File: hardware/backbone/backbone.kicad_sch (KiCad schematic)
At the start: 68 parts, among them J1 M20-7810645R, J140 M20-7810645R, J2 FROM_PREVIOUS, J3 M20-7810645R, J4 SM04B-SRSS-TB(LF)(SN), J5 FH12-24S-0.5SH(55), J9 TO NEXT, Q2 AO3401A, U1 ESP32-S3-WROOM-1_1U_FlexyPin_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, U10 ME6211C15M5G-N, U11 SN74LVC1G125DBVR, U2 SN65HVD230DR, U3 HC-TYPE-C-16P-01A, U4 AP2112K-3.3TRG1, U5 AP2112K-3.3TRG1, U8 G3VM-61VY3, U9 ME6211C28M5G-N

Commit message: Use power symbols and generic FPC expansion names
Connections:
- net CAM_1V5 renamed +1V5
- net CAM_2V8 renamed +2V8
- net CAM_PWDN renamed FPC_PULLDOWN
- net CAM_RESET_N renamed FPC_PULLUP
- net CAM_XCLK renamed FPC_CLK
- net CAM_XCLK_DRV renamed FPC_CLK_DRV
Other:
- note added: "+1V5"
- note added: "+2V8"
- note added: "AUXILIARY 1.5 V REGULATOR"
- note added: "AUXILIARY 2.8 V REGULATOR"
- note added: "BUFFERED CLOCK - 3.3 V TO 2.8 V"
- note added: "Buffer GPIO15; place R30 close to U11 output."
- note added: "C79/C80: +2V8 decoupling. C81: +1V5 decoupling."
- note added: "CLK_OUT"
- note added: "Check peripheral pinout, voltages and flex orientation."
- note added: "EXPANSION - 24-PIN FPC"
- note added: "FPC BIAS RESISTORS"
- note added: "FPC shares I2C on GPIO4/5; pull-ups to 3.3 V."
- note added: "FPC signals, fixed bias pins and voltage limits: see project documentation."
- note added: "FPC_PULLDOWN: 10k to GND"
- note added: "FPC_PULLUP: 10k to +2V8"
- note added: "Fixed auxiliary rails: 2.8 V / 1.5 V. Check peripheral voltage requirements."
- note added: "Fixed pull-up / pull-down; no MCU control assigned."
- note added: "GPIO1"
- note added: "GPIO17"
- note added: "GPIO18"
- note added: "GPIO2"
- note added: "GPIO21"
- note added: "GPIO38"
- note added: "GPIO39"
- note added: "GPIO40"
- note added: "GPIO41"
- note added: "GPIO42"
- note added: "GPIO6"
- note added: "PULLDOWN"
- note added: "PULLUP"
- note removed: "AVDD 2.8V"
- note removed: "Buffer XCLK; place R30 close to U11 output."
- note removed: "C79: AVDD; C80: DOVDD; C81: DVDD."
- note removed: "CAMERA 1.5 V REGULATOR"
- note removed: "CAMERA 2.8 V REGULATOR"
- note removed: "CAMERA CLOCK - 3.3 V TO 2.8 V"
- note removed: "CAMERA CONTROL DEFAULTS"
- note removed: "CAMERA DVP - 24-PIN FPC"
- note removed: "Camera SCCB shares GPIO4/5 directly; pull-ups to 3.3 V."
- note removed: "D0 / Y2"
- note removed: "D1 / Y3"
- note removed: "D2 / Y4"
- note removed: "D3 / Y5"
- note removed: "D4 / Y6"
- note removed: "D5 / Y7"
- note removed: "D6 / Y8"
- note removed: "D7 / Y9"
- note removed: "DOVDD 2.8V"
- note removed: "DVDD 1.5V"
- note removed: "ESP32-S3-EYE pinout. Verify the actual flex orientation."
- note removed: "Fixed camera rails: 2.8 V / 1.5 V. Qualify each camera module before use."
- note removed: "GPIO assignments and electrical limits: hardware/backbone/CAMERA-V3.md"
- note removed: "HREF"
- note removed: "No MCU GPIO assigned to RESET or PWDN."
- note removed: "PCLK"
- note removed: "PWDN"
- note removed: "PWDN: low = active"
- note removed: "RESET_N"
- note removed: "RESET_N: high = run"
- note removed: "VSYNC"
- note removed: "XCLK"

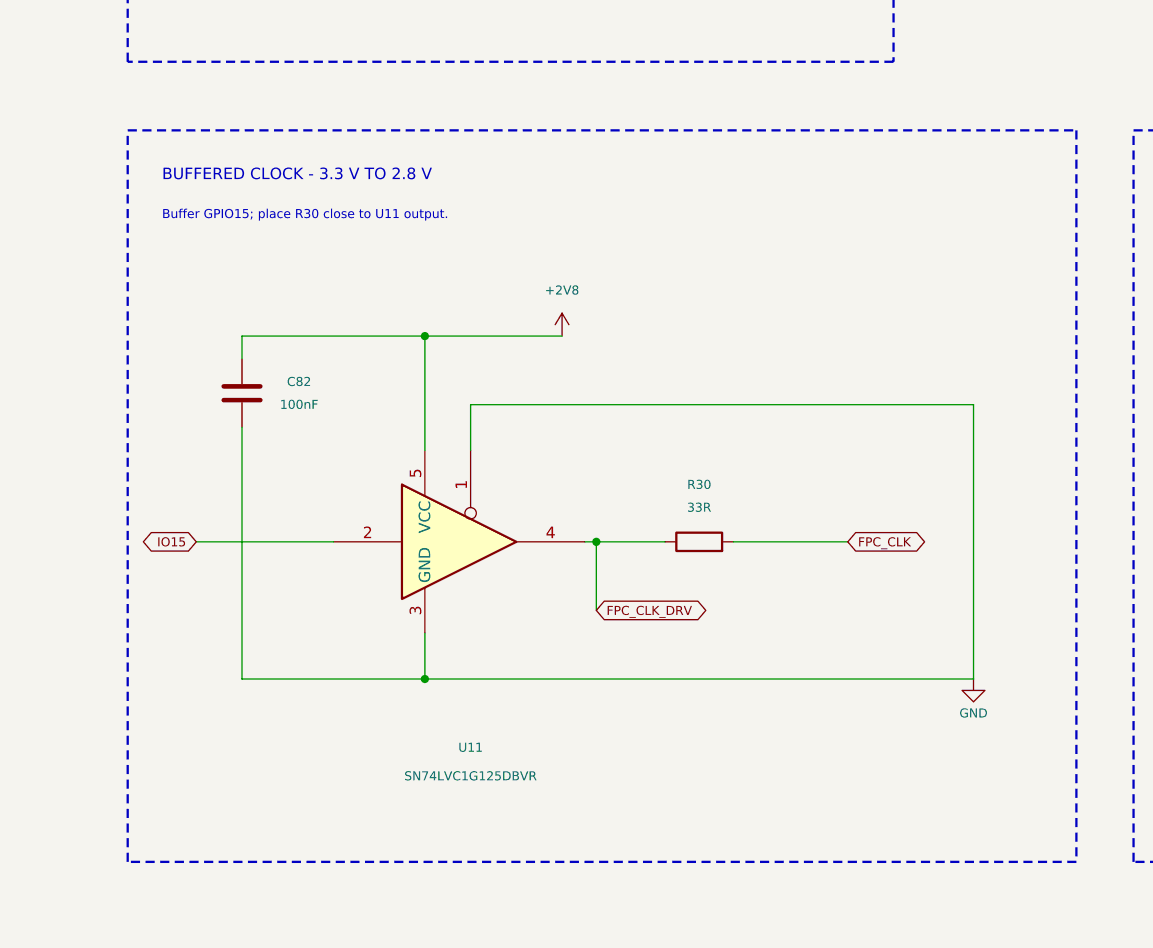
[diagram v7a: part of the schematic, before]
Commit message: Match Espressif camera clock path without added buffer
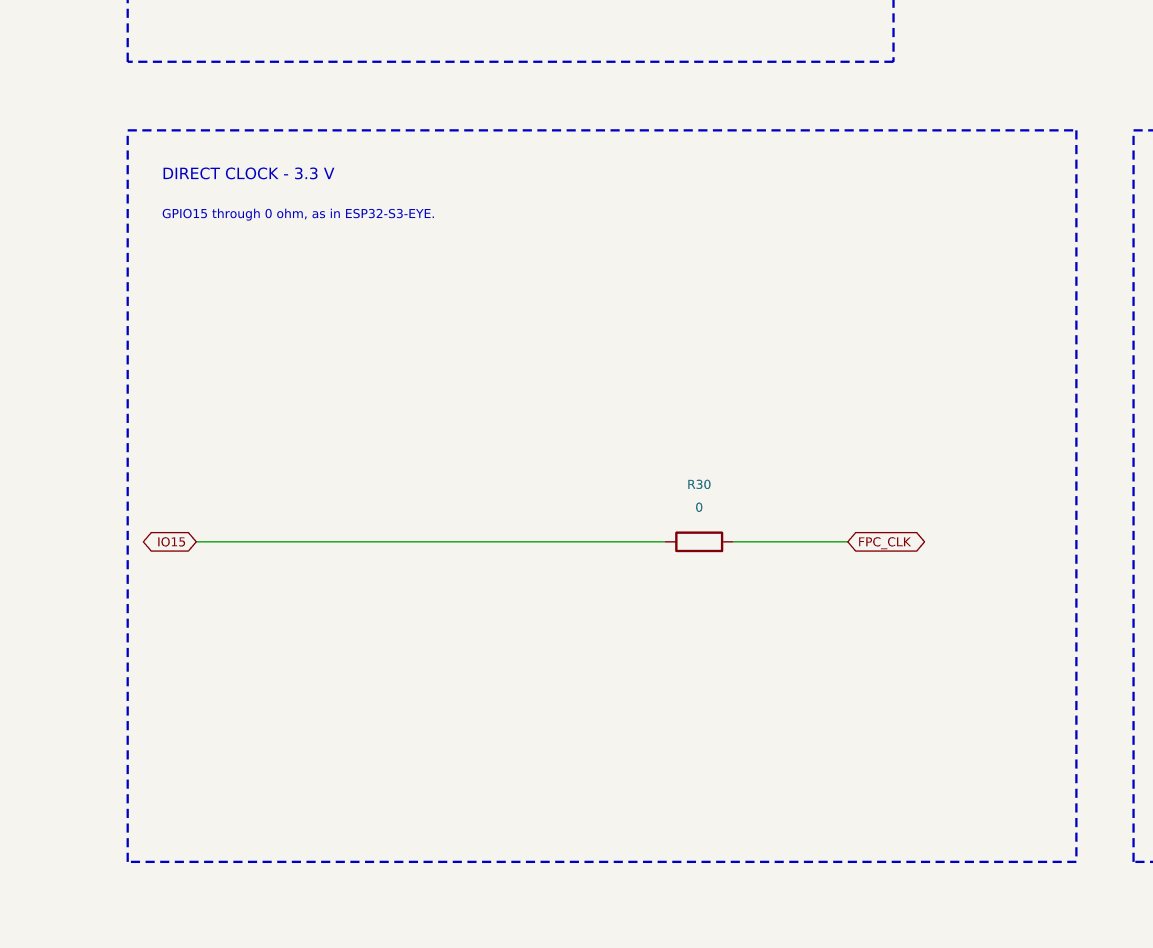
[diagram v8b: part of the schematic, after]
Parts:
- removed C82: 100nF, SpaghettiLAB:C0603, symbol Device:C
- removed U11: SN74LVC1G125DBVR, Package_TO_SOT_SMD:SOT-23-5, symbol SpaghettiLAB:SN74LVC1G125DBVR
- R30: value 33R -> 0
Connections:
- net FPC_CLK_DRV is gone; now on net IO15: R30.1
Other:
- note added: "DIRECT CLOCK - 3.3 V"
- note added: "GPIO15 through 0 ohm, as in ESP32-S3-EYE."
- note removed: "BUFFERED CLOCK - 3.3 V TO 2.8 V"
- note removed: "Buffer GPIO15; place R30 close to U11 output."
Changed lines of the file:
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@@
-)
-(symbol
-  (lib_id "SpaghettiLAB:SN74LVC1G125DBVR")
-  (at 335.28 307.34 0)
-  (unit 1)
-  (in_bom yes)
-  (on_board yes)
-  (dnp no)
-  (property "Reference" "U11"
-    (at 335.28 330.2 0)
-    (effects
-      (font
-        (size 1 1)
-      )
-    )
-  )
-  (property "Value" "SN74LVC1G125DBVR"
-    (at 335.28 333.375 0)
-    (effects
-      (font
-        (size 1 1)
-      )
-    )
-  )
-  (property "Footprint" "Package_TO_SOT_SMD:SOT-23-5"
-    (at 335.28 307.34 0)
-    (effects
-      (font
-        (size 1.0 1.0)
-      )
-      (hide yes)
-    )
-  )
-  (property "Datasheet" "https://www.ti.com/lit/ds/symlink/sn74lvc1g125.pdf"
-    (at 335.28 307.34 0)
-    (effects
-      (font
-        (size 1.0 1.0)
-      )
-      (hide yes)
-    )
-  )
-  (pin "1"
-  )
-  (pin "2"
-  )
-  (pin "3"
-  )
-  (pin "4"
-  )
-  (pin "5"
-  )
-  (instances
-    (project "backbone"
-      (path "/9262d91e-b0ff-47b4-bf11-6f94636af855"
-        (reference "U11")
-        (unit 1)
-      )
-    )
-  )
 )
 (symbol
@@
     )
   )
-  (property "Value" "33R"
+  (property "Value" "0"
     (at 360.68 303.53 90)
     (effects
@@
       (path "/9262d91e-b0ff-47b4-bf11-6f94636af855"
         (reference "C81")
-        (unit 1)
-      )
-    )
-  )
-)
-(symbol
-  (lib_id "Device:C")
-  (at 309.88 290.83 0)
-  (unit 1)
-  (in_bom yes)
-  (on_board yes)
-  (dnp no)
-  (property "Reference" "C82"
-    (at 316.23 289.56 0)
-    (effects
-      (font
-        (size 1 1)
-      )
-    )
-  )
-  (property "Value" "100nF"
-    (at 316.23 292.1 0)
-    (effects
-      (font
-        (size 1 1)
-      )
-    )
-  )
-  (property "Footprint" "SpaghettiLAB:C0603"
-    (at 309.88 290.83 0)
-    (effects
-      (font
-        (size 1.0 1.0)
-      )
-      (hide yes)
-    )
-  )
-  (property "Datasheet" ""
-    (at 309.88 290.83 0)
-    (effects
-      (font
-        (size 1.0 1.0)
-      )
-      (hide yes)
-    )
-  )
-  (pin "1"
-  )
-  (pin "2"
-  )
-  (instances
-    (project "backbone"
-      (path "/9262d91e-b0ff-47b4-bf11-6f94636af855"
-        (reference "C82")
         (unit 1)
       )
@@
 (symbol (lib_id "power:GND") (at 345.44 224.79 0) (unit 1) (in_bom no) (on_board no) (dnp no) (property "Reference" "#PWR0176" (at 345.44 224.79 0) (effects (font (size 1 1)) (hide yes))) (property "Value" "GND" (at 351.79 227.33 0) (effects (font (size 1 1)))) (pin "1") (instances (project "backbone" (path "/9262d91e-b0ff-47b4-bf11-6f94636af855" (reference "#PWR0176") (unit 1)))))
 (rectangle (start 297.18 261.62) (end 402.59 342.9) (stroke (width 0.254) (type dash)) (fill (type none)))
-(text "BUFFERED CLOCK - 3.3 V TO 2.8 V" (at 300.99 266.7 0) (effects (font (size 1.27 1.27)) (justify left)))
-(text "Buffer GPIO15; place R30 close to U11 output." (at 300.99 271.15 0) (effects (font (size 1 1)) (justify left)))
-(global_label "IO15" (shape bidirectional) (at 304.8 307.34 180) (effects (font (size 1 1)) (justify right)))
-(global_label "FPC_CLK" (shape bidirectional) (at 377.19 307.34 0) (effects (font (size 1 1)) (justify left)))
-(global_label "FPC_CLK_DRV" (shape bidirectional) (at 349.25 314.96 0) (effects (font (size 1 1)) (justify left)))
-(symbol (lib_id "power:+2V8") (at 345.44 284.48 0) (unit 1) (in_bom no) (on_board no) (dnp no) (property "Reference" "#PWR0177" (at 345.44 284.48 0) (effects (font (size 1 1)) (hide yes))) (property "Value" "+2V8" (at 345.44 279.4 0) (effects (font (size 1 1)))) (pin "1") (instances (project "backbone" (path "/9262d91e-b0ff-47b4-bf11-6f94636af855" (reference "#PWR0177") (unit 1)))))
-(symbol (lib_id "power:GND") (at 391.16 322.58 0) (unit 1) (in_bom no) (on_board no) (dnp no) (property "Reference" "#PWR0178" (at 391.16 322.58 0) (effects (font (size 1 1)) (hide yes))) (property "Value" "GND" (at 391.16 326.39 0) (effects (font (size 1 1)))) (pin "1") (instances (project "backbone" (path "/9262d91e-b0ff-47b4-bf11-6f94636af855" (reference "#PWR0178") (unit 1)))))
+(text "DIRECT CLOCK - 3.3 V" (at 300.99 266.7 0) (effects (font (size 1.27 1.27)) (justify left)))
+(text "GPIO15 through 0 ohm, as in ESP32-S3-EYE." (at 300.99 271.15 0) (effects (font (size 1 1)) (justify left)))
 (rectangle (start 408.94 261.62) (end 480.06 342.9) (stroke (width 0.254) (type dash)) (fill (type none)))
 (text "FPC BIAS RESISTORS" (at 412.75 266.7 0) (effects (font (size 1.27 1.27)) (justify left)))
@@
 (text "Fixed auxiliary rails: 2.8 V / 1.5 V. Check peripheral voltage requirements." (at 302.26 355.6 0) (effects (font (size 1 1)) (justify left)))
 (text "FPC signals, fixed bias pins and voltage limits: see project documentation." (at 302.26 360.68 0) (effects (font (size 1 1)) (justify left)))
-(wire (pts (xy 304.8 307.34) (xy 320.04 307.34)) (stroke (width 0) (type default)))
 (wire (pts (xy 309.88 198.12) (xy 320.04 198.12)) (stroke (width 0) (type default)))
 (wire (pts (xy 309.88 229.87) (xy 320.04 229.87)) (stroke (width 0) (type default)))
 (wire (pts (xy 309.88 232.41) (xy 337.82 232.41)) (stroke (width 0) (type default)))
-(wire (pts (xy 309.88 284.48) (xy 309.88 287.02)) (stroke (width 0) (type default)))
-(wire (pts (xy 309.88 284.48) (xy 330.2 284.48)) (stroke (width 0) (type default)))
-(wire (pts (xy 309.88 294.64) (xy 309.88 322.58)) (stroke (width 0) (type default)))
-(wire (pts (xy 309.88 322.58) (xy 330.2 322.58)) (stroke (width 0) (type default)))
 (wire (pts (xy 320.04 198.12) (xy 320.04 204.47)) (stroke (width 0) (type default)))
 (wire (pts (xy 320.04 198.12) (xy 337.82 198.12)) (stroke (width 0) (type default)))
 (wire (pts (xy 320.04 212.09) (xy 320.04 229.87)) (stroke (width 0) (type default)))
 (wire (pts (xy 320.04 229.87) (xy 360.68 229.87)) (stroke (width 0) (type default)))
-(wire (pts (xy 330.2 284.48) (xy 330.2 297.18)) (stroke (width 0) (type default)))
-(wire (pts (xy 330.2 284.48) (xy 345.44 284.48)) (stroke (width 0) (type default)))
-(wire (pts (xy 330.2 317.5) (xy 330.2 322.58)) (stroke (width 0) (type default)))
-(wire (pts (xy 330.2 322.58) (xy 391.16 322.58)) (stroke (width 0) (type default)))
-(wire (pts (xy 335.28 292.1) (xy 335.28 297.18)) (stroke (width 0) (type default)))
-(wire (pts (xy 335.28 292.1) (xy 391.16 292.1)) (stroke (width 0) (type default)))
 (wire (pts (xy 337.82 198.12) (xy 337.82 204.47)) (stroke (width 0) (type default)))
 (wire (pts (xy 337.82 198.12) (xy 350.52 198.12)) (stroke (width 0) (type default)))
@@
 (wire (pts (xy 337.82 232.41) (xy 360.68 232.41)) (stroke (width 0) (type default)))
 (wire (pts (xy 345.44 224.79) (xy 350.52 224.79)) (stroke (width 0) (type default)))
-(wire (pts (xy 347.98 307.34) (xy 349.25 307.34)) (stroke (width 0) (type default)))
-(wire (pts (xy 349.25 307.34) (xy 349.25 314.96)) (stroke (width 0) (type default)))
-(wire (pts (xy 349.25 307.34) (xy 356.87 307.34)) (stroke (width 0) (type default)))
 (wire (pts (xy 350.52 198.12) (xy 350.52 204.47)) (stroke (width 0) (type default)))
 (wire (pts (xy 350.52 198.12) (xy 358.14 198.12)) (stroke (width 0) (type default)))
@@
 (wire (pts (xy 358.14 198.12) (xy 358.14 227.33)) (stroke (width 0) (type default)))
 (wire (pts (xy 358.14 227.33) (xy 360.68 227.33)) (stroke (width 0) (type default)))
-(wire (pts (xy 364.49 307.34) (xy 377.19 307.34)) (stroke (width 0) (type default)))
 (wire (pts (xy 389.89 58.42) (xy 397.51 58.42)) (stroke (width 0) (type default)))
-(wire (pts (xy 391.16 292.1) (xy 391.16 322.58)) (stroke (width 0) (type default)))
 (wire (pts (xy 397.51 58.42) (xy 397.51 62.23)) (stroke (width 0) (type default)))
 (wire (pts (xy 397.51 69.85) (xy 397.51 81.28)) (stroke (width 0) (type default)))
@@
 (junction (at 350.52 198.12) (diameter 0) (color 0 0 0 0))
 (junction (at 500.38 247.65) (diameter 0) (color 0 0 0 0))
-(junction (at 330.2 284.48) (diameter 0) (color 0 0 0 0))
-(junction (at 349.25 307.34) (diameter 0) (color 0 0 0 0))
 (junction (at 492.76 257.81) (diameter 0) (color 0 0 0 0))
 (junction (at 337.82 232.41) (diameter 0) (color 0 0 0 0))
@@
 (junction (at 520.7 81.28) (diameter 0) (color 0 0 0 0))
 (junction (at 560.07 325.12) (diameter 0) (color 0 0 0 0))
-(junction (at 330.2 322.58) (diameter 0) (color 0 0 0 0))
 (junction (at 443.23 58.42) (diameter 0) (color 0 0 0 0))
 (junction (at 500.38 325.12) (diameter 0) (color 0 0 0 0))
@@
 (wire (pts (xy 402.59 58.42) (xy 407.67 58.42)) (stroke (width 0) (type default)))
 (junction (at 402.59 58.42) (diameter 0) (color 0 0 0 0))
-)
+(wire (pts (xy 304.8 307.34) (xy 356.87 307.34)) (stroke (width 0) (type default)))
+(wire (pts (xy 364.49 307.34) (xy 377.19 307.34)) (stroke (width 0) (type default)))
+(global_label "IO15" (shape bidirectional) (at 304.8 307.34 180) (effects (font (size 1 1)) (justify right)))
+(global_label "FPC_CLK" (shape bidirectional) (at 377.19 307.34 0) (effects (font (size 1 1)) (justify left)))
+)
